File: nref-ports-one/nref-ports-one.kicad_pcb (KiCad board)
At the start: 4 copper layers, 88 x 35.5 mm, 116 parts, among them J1 CONN_HEAD, J10 CONN_SPK, J2 DM3AT-SF-PEJM5, J3 09452812561, J4 USB_C_Receptacle, J5 Conn_01x10_Pin, J6 Conn_01x14_Pin, J7 Conn_01x12_Pin, J8 PWR, J9 Conn_01x10_Pin, U1 TPS7A0533PDBZ, U12 TLV75518PDBV, U2 TLV320AIC3100, U3 TXS0108EPW, U4 SN74AVC1T45, U5 TPD4E02B04DQA, U6 TPD4E02B04DQA, U7 TPD4E02B04DQA, U8 FUSB302BMPX, U9 AP22815A

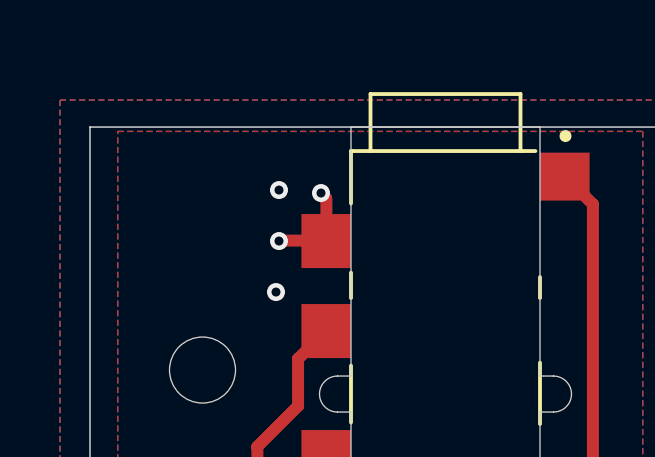
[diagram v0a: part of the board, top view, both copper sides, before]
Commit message: ports-one: schematics with new mux, local 5v, hard reset switch
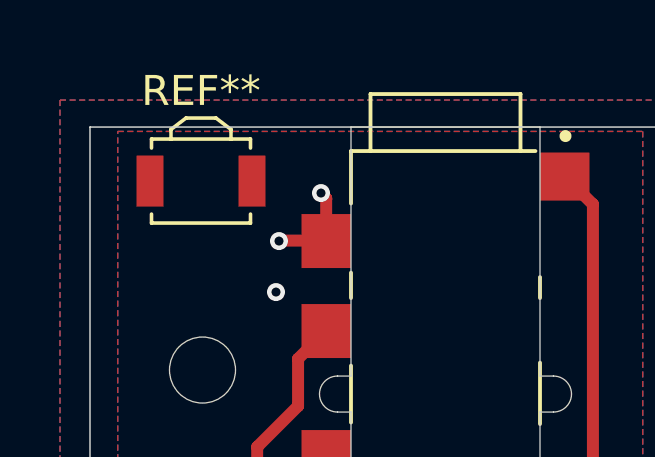
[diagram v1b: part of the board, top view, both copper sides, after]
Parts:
- added REF**: SW_SPST_B3U-3000P, Button_Switch_SMD:SW_SPST_B3U-3000P, F.Cu at (103.7, 103.7)
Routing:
- net GNDA: vias 22 -> 21

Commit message: ports-one: add redriver, routing WIP
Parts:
- removed FB10: 100@100MHz 3A, Inductor_SMD:L_0603_1608Metric
- removed REF**: SW_SPST_B3U-3000P, Button_Switch_SMD:SW_SPST_B3U-3000P
- added C45: 0.1uF, Capacitor_SMD:C_0402_1005Metric, F.Cu at (161.7, 149.2)
- added C46: 47uF, Capacitor_SMD:C_1210_3225Metric, F.Cu at (178.8, 142.3)
- added C47: 10uF, Capacitor_SMD:C_0603_1608Metric, F.Cu at (173.3, 138.6)
- added D4: LED_Blue, LED_SMD:LED_0603_1608Metric, F.Cu at (183.9, 103.7)
- added J11: POWSW, Connector_JST:JST_SH_SM02B-SRSS-TB_1x02-1MP_P1.00mm_Horizontal, F.Cu at (102.8, 131.8)
- added L4: 6.8uH, Inductor_SMD:L_Taiyo-Yuden_NR-30xx, F.Cu at (175.3, 142.2)
- added R36: 0, Resistor_SMD:R_0402_1005Metric, F.Cu at (183.8, 116.0)
- added R37: 13.7k, Resistor_SMD:R_0402_1005Metric, F.Cu at (168.7, 142.2)
- added R38: 10k, Resistor_SMD:R_0402_1005Metric, F.Cu at (166.4, 140.8)
- added R39: 0, Resistor_SMD:R_0402_1005Metric, F.Cu at (164.0, 120.5)
- added R40: 0, Resistor_SMD:R_0603_1608Metric, F.Cu at (173.1, 130.2)
- added R41: 0, Resistor_SMD:R_0402_1005Metric, F.Cu at (164.0, 121.5)
- added SW1: SW_Push, Button_Switch_SMD:SW_SPST_B3U-3000P, F.Cu at (103.8, 104.0)
- added TP1: TestPoint, TestPoint:TestPoint_Pad_D1.0mm, F.Cu at (194.4, 124.2)
- added TP2: TestPoint, TestPoint:TestPoint_Pad_D1.0mm, F.Cu at (194.4, 127.3)
- added TP3: TestPoint, TestPoint:TestPoint_Pad_D1.0mm, F.Cu at (194.4, 130.3)
- added U10: LMR51430, Package_TO_SOT_SMD:SOT-23-6, F.Cu at (171.3, 141.2)
- added U11: TPS66021YBGR, footprints:YBG0028_TEX, F.Cu at (176.9, 125.2)
- added U13: TMUXHS4212, footprints:Texas-VQFN20_2.5x4.5mm_RKS, F.Cu at (173.6, 120.5)
- added U14: EQCO5X31C0-I_6NX, footprints:QFN50P400X400X100-21N-D, F.Cu at (167.2, 131.8)
- C17, C21, C39, C40: footprint Capacitor_SMD:C_1206_3216Metric -> Capacitor_SMD:C_1210_3225Metric
- C38: value 47uF -> 0.1uF; footprint Capacitor_SMD:C_1206_3216Metric -> Capacitor_SMD:C_0402_1005Metric
- C41: value 0.1uF -> 10uF; footprint Capacitor_SMD:C_0402_1005Metric -> Capacitor_SMD:C_0603_1608Metric
- C8: value 0.1uF -> 1uF
- D1, D2: value LED_Small -> LED_Red
- D3: value SS54 -> LED_Red; footprint Diode_SMD:D_SMA -> LED_SMD:LED_0603_1608Metric
- J4: footprint footprints:MOLEX_105450-0101 -> Connector_USB:USB_C_Receptacle_Molex_105450-0101
- R23: value 200k -> 10k
- R25: value 200k -> 75k 1%
- R26: value 200k -> 0
- R27: value 200k -> 432k 1%
- R28: value 10k -> 20k 1%
- R29: value 900k -> 0
- R30: value 200k -> 2.2k
- R31: value 0 -> 2.2k
- R32, R33: value 0 -> 1k
- R34: value 10k -> 0
- R35: value 0 -> 100k
- U9: value AP22815A -> PCA9557BS; footprint Package_TO_SOT_SMD:SOT-23-5 -> Package_DFN_QFN:HVQFN-16-1EP_3x3mm_P0.5mm_EP1.5x1.5mm
- moved R34 49.0 mm to (115.2, 141.7), turned to 0 degrees
- moved C41 33.4 mm to (187.2, 144.8)
- moved R32 28.6 mm to (186.9, 104.3), turned to 90 degrees
- moved R24 28.2 mm to (184.1, 145.1), turned to 0 degrees
- moved C38 28.1 mm to (161.7, 147.2), turned to 0 degrees
- moved R21 27.9 mm to (159.1, 124.3)
- moved R29 26.4 mm to (182.1, 146.3)
- moved R33 25.0 mm to (183.7, 105.8), turned to 0 degrees
- moved R20 25.0 mm to (160.2, 124.3)
- moved D3 24.4 mm to (185.6, 103.7)
- moved R35 23.9 mm to (168.7, 140.3), turned to 90 degrees
- moved R31 21.7 mm to (156.2, 119.7), turned to -90 degrees
- moved C32 21.3 mm to (161.7, 145.2), turned to 0 degrees
- moved C40 19.4 mm to (177.8, 128.8), turned to 180 degrees
- moved R19 18.5 mm to (158.0, 124.3), turned to -90 degrees
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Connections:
- C32 pad 1: +5V -> Net-(U11-VIN)
- C37 pad 2: STANDBY_3V3 -> LDO_3V3
- C38 pad 1: MUX_5V -> Net-(U10-CB)
- C38 pad 2: GND -> Net-(U10-SW)
- C40 pad 1: USB_VBUS -> VPD
- C41 pad 1: STANDBY_3V3 -> Net-(U11-VLDO)
- C42 pad 1: MUX_3V3 -> /MUX_3V3
- C8 pad 1: +5V -> Net-(U1-VI)
- D3 pad 1: VPD -> Net-(D3-K)
- D3 pad 2: USB_VBUS -> Net-(D3-A)
- FB7 pad 1: +5V -> 5V_AUX
- R19 pad 1: Net-(U9-FLG) -> USB_SINK_EN
- R19 pad 2: +5V -> LDO_3V3
- R20 pad 1: CC2 -> ~{USB_MUX_OE}
- R21 pad 1: CC1 -> USB_MUX_DIR
- R22 pad 1: MUX_3V3 -> /MUX_3V3
- R22 pad 2: +3V3 -> STANDBY_3V3
- R23 pad 1: Net-(U10-DIR) -> GND
- R23 pad 2: MUX_3V3 -> USB_SRC_EN
- R24 pad 1: MUX_5V -> LDO_3V3
- R24 pad 2: +5V -> Net-(U11-VLDO)
- R25 pad 2: MUX_5V -> GND
- R26 pad 1: Net-(U10-~{INT_N}/OUT3) -> 5V_AUX
- R26 pad 2: MUX_5V -> Net-(U11-VIN)
- R27 pad 1: Net-(U10-VCONN_FAULT_N) -> Net-(U11-OVP)
- R27 pad 2: MUX_5V -> USB_VBUS
- R28 pad 1: MUX_5V -> Net-(U11-OVP)
- R28 pad 2: Net-(U10-CURRENT_MODE) -> GND
- R29 pad 1: USB_VBUS -> STANDBY_3V3
- R29 pad 2: Net-(U10-VBUS_DET) -> LDO_3V3
- R30 pad 1: USB_VBUS -> STANDBY_3V3
- R30 pad 2: Net-(U10-PORT) -> Net-(U9-~{RESET})
- R31 pad 1: GND -> STANDBY_3V3
- R31 pad 2: Net-(U10-~{ENN_MUX}) -> Net-(U9-A0)
- R32 pad 1: Net-(U10-SCL/OUT2) -> STANDBY_3V3
- R32 pad 2: RP_SCL0 -> Net-(D3-A)
- R33 pad 1: Net-(U10-SDA/OUT1) -> STANDBY_3V3
- R33 pad 2: RP_SDA0 -> Net-(D4-A)
- R34 pad 1: STANDBY_3V3 -> 5V_AUX
- R34 pad 2: Net-(U11-~{RESET}) -> Net-(U1-VI)
- R35 pad 1: GND -> 5V_AUX
- U1 pad 3: +5V -> Net-(U1-VI)
- U6 pad 1: USBH_2A_RXN -> /USBH_2A_AC_TXN
- U6 pad 10: USBH_2A_RXN -> /USBH_2A_AC_TXN
- U6 pad 2: USBH_2A_RXP -> /USBH_2A_AC_TXP
- U6 pad 4: /USBH_2A_AC_TXN -> USBH_2A_RXN
- U6 pad 5: /USBH_2A_AC_TXP -> USBH_2A_RXP
- U6 pad 6: /USBH_2A_AC_TXP -> USBH_2A_RXP
- U6 pad 7: /USBH_2A_AC_TXN -> USBH_2A_RXN
- U6 pad 9: USBH_2A_RXP -> /USBH_2A_AC_TXP
- U8 pad 12: unconnected-(U8-VCONN-Pad12) -> Net-(R36-Pad2)
- U8 pad 13: unconnected-(U8-VCONN-Pad13) -> Net-(R36-Pad2)
- U8 pad 3: STANDBY_3V3 -> LDO_3V3
- U8 pad 4: STANDBY_3V3 -> LDO_3V3
- U9 pad 1: USB_VBUS -> Net-(U9-A0)
- U9 pad 3: Net-(U9-FLG) -> GND
- U9 pad 5: +5V -> USB_SINK_EN
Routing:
- net +3V3: track 156.6 -> 35.1 mm, vias 6 -> 3
- net +5V: track 82.4 -> 16.4 mm, vias 3 -> 1
- net USB1_TXN: track 0.00 -> 55.4 mm
- net USB1_TXP: track 0.00 -> 54.3 mm
- net USB1_RXN: track 0.00 -> 51.4 mm, vias 1 -> 0
- net USB1_RXP: track 0.00 -> 50.8 mm
- net +1V8: track 49.9 -> 8.60 mm
- net GND: track 89.8 -> 51.1 mm, vias 66 -> 39
- net ETH0_LED_LINK1: track 32.9 -> 0.00 mm
- net DAC_SDA: track 34.9 -> 3.16 mm
- net DAC_SCL: track 35.1 -> 3.67 mm
- net ETH0_LED_RX: track 30.4 -> 0.00 mm
- net USB_VBUS: track 38.0 -> 12.4 mm, vias 7 -> 3
- net Net-(U13-SEL): track 23.4 -> 0.00 mm, vias 1 -> 0
- net Net-(U2-DIN): track 26.0 -> 2.70 mm
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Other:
- board text added: "TODO: caps might be too high"

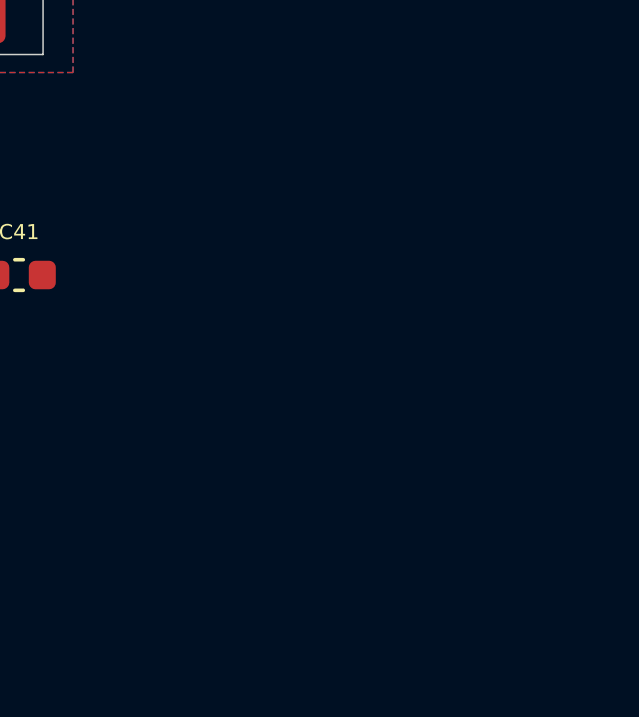
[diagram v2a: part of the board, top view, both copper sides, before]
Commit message: ports-one: add redriver circuit
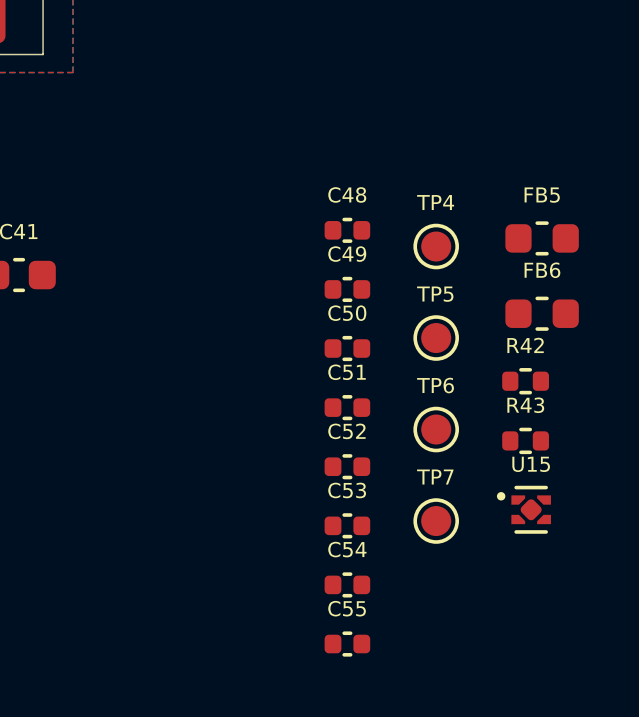
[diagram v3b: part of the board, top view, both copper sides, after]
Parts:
- added C48: 1uF, Capacitor_SMD:C_0402_1005Metric, F.Cu at (198.1, 143.3)
- added C49: 1uF, Capacitor_SMD:C_0402_1005Metric, F.Cu at (198.1, 145.2)
- added C50: 4.7uF, Capacitor_SMD:C_0402_1005Metric, F.Cu at (198.1, 147.2)
- added C51: 4.7uF, Capacitor_SMD:C_0402_1005Metric, F.Cu at (198.1, 149.2)
- added C52: 0.1uF, Capacitor_SMD:C_0402_1005Metric, F.Cu at (198.1, 151.1)
- added C53: 1uF, Capacitor_SMD:C_0402_1005Metric, F.Cu at (198.1, 153.1)
- added C54: 1uF, Capacitor_SMD:C_0402_1005Metric, F.Cu at (198.1, 155.1)
- added C55: 0.1uF, Capacitor_SMD:C_0402_1005Metric, F.Cu at (198.1, 157.1)
- added FB5: 100@100MHz 3A, Inductor_SMD:L_0603_1608Metric, F.Cu at (204.6, 143.5)
- added FB6: 100@100MHz 3A, Inductor_SMD:L_0603_1608Metric, F.Cu at (204.6, 146.0)
- added R42: 0, Resistor_SMD:R_0402_1005Metric, F.Cu at (204.1, 148.3)
- added R43: 0, Resistor_SMD:R_0402_1005Metric, F.Cu at (204.1, 150.3)
- added TP4: TestPoint, TestPoint:TestPoint_Pad_D1.0mm, F.Cu at (201.1, 143.8)
- added TP5: TestPoint, TestPoint:TestPoint_Pad_D1.0mm, F.Cu at (201.1, 146.8)
- added TP6: TestPoint, TestPoint:TestPoint_Pad_D1.0mm, F.Cu at (201.1, 149.9)
- added TP7: TestPoint, TestPoint:TestPoint_Pad_D1.0mm, F.Cu at (201.1, 152.9)
- added U15: LP5907MFX-1.2, Package_SON:Texas_X2SON-4_1x1mm_P0.65mm, F.Cu at (204.3, 152.6)
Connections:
- U14 pad 10: unconnected-(U14-TSI-Pad10) -> Net-(U14-TSI)
- U14 pad 11: unconnected-(U14-LOM-Pad11) -> Net-(U14-LOM)
- U14 pad 14: unconnected-(U14-VCCB-Pad14) -> +1V2
- U14 pad 15: unconnected-(U14-PLLB1-Pad15) -> Net-(U14-PLLB1)
- U14 pad 16: unconnected-(U14-PLLB2-Pad16) -> Net-(U14-PLLB2)
- U14 pad 20: unconnected-(U14-TEST0-Pad20) -> Net-(U14-TEST0)
- U14 pad 4: unconnected-(U14-VCCA-Pad4) -> +1V2
- U14 pad 5: unconnected-(U14-PLLA1-Pad5) -> Net-(U14-PLLA1)
- U14 pad 6: unconnected-(U14-PLLA2-Pad6) -> Net-(U14-PLLA2)
- U14 pad 7: unconnected-(U14-TSC-Pad7) -> Net-(U14-TSC)

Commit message: ports-one: routing snapshot
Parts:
- removed R24: 0, Resistor_SMD:R_0402_1005Metric
- removed TP7: TestPoint, TestPoint:TestPoint_Pad_D1.0mm
- FB1, FB2, FB3, FB4, FB5, FB6, FB7, FB8, FB9: footprint Inductor_SMD:L_0603_1608Metric -> Inductor_SMD:L_0402_1005Metric
- moved FB5 43.8 mm to (163.5, 128.3), turned to 90 degrees
- moved TP1 42.4 mm to (152.3, 119.5)
- moved TP2 41.6 mm to (153.2, 121.0)
- moved TP6 41.5 mm to (167.8, 125.2)
- moved C53 41.1 mm to (165.4, 128.3), turned to 90 degrees
- moved TP4 40.8 mm to (162.4, 130.7)
- moved TP5 40.7 mm to (166.2, 125.9)
- moved C52 40.7 mm to (164.4, 128.3), turned to 90 degrees
- moved R43 40.3 mm to (169.2, 130.1), turned to 90 degrees
- moved C50 40.2 mm to (162.5, 128.7), turned to -90 degrees
- moved U15 37.5 mm to (171.5, 134.2), turned to 180 degrees
- moved FB6 37.4 mm to (168.7, 135.6), turned to 90 degrees
- moved C55 37.2 mm to (167.8, 135.6), turned to -90 degrees
- moved C54 36.9 mm to (166.8, 135.6), turned to -90 degrees
- moved R42 36.0 mm to (171.6, 132.9)
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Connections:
- net USBH_2B_TXN renamed USB_A_TXN
- net USBH_2B_TXP renamed USB_A_TXP
- C33 pad 1: /USBH_2A_AC_TXN -> /USB_B_AC_TXN
- C33 pad 2: USBH_2A_TXN -> USB_B_TXN
- C34 pad 1: /USBH_2B_AC_TXN -> /USB_A_AC_TXN
- C35 pad 1: /USBH_2A_AC_TXP -> /USB_B_AC_TXP
- C35 pad 2: USBH_2A_TXP -> USB_B_TXP
- C36 pad 1: /USBH_2B_AC_TXP -> /USB_A_AC_TXP
- C41 pad 1: Net-(U11-VLDO) -> LDO_3V3
- J4 pad A10: USBH_2B_RXN -> USB_A_RXN
- J4 pad A11: USBH_2B_RXP -> USB_A_RXP
- J4 pad A2: /USBH_2A_AC_TXP -> /USB_B_AC_TXP
- J4 pad A3: /USBH_2A_AC_TXN -> /USB_B_AC_TXN
- J4 pad B10: USBH_2A_RXN -> USB_B_RXN
- J4 pad B11: USBH_2A_RXP -> USB_B_RXP
- J4 pad B2: /USBH_2B_AC_TXP -> /USB_A_AC_TXP
- J4 pad B3: /USBH_2B_AC_TXN -> /USB_A_AC_TXN
- U11 pad G3: Net-(U11-VLDO) -> LDO_3V3
- U13 pad 12: USBH_2A_TXN -> USB_B_TXP
- U13 pad 13: USBH_2A_TXP -> USB_B_TXN
- U13 pad 14: USBH_2B_RXN -> USB_B_RXP
- U13 pad 15: USBH_2B_RXP -> USB_B_RXN
- U13 pad 18: USBH_2A_RXN -> USB_A_RXN
- U13 pad 19: USBH_2A_RXP -> USB_A_RXP
- U6 pad 1: /USBH_2A_AC_TXN -> USB_B_RXN
- U6 pad 10: /USBH_2A_AC_TXN -> USB_B_RXN
- U6 pad 2: /USBH_2A_AC_TXP -> USB_B_RXP
- U6 pad 4: USBH_2A_RXN -> /USB_B_AC_TXN
- U6 pad 5: USBH_2A_RXP -> /USB_B_AC_TXP
- U6 pad 6: USBH_2A_RXP -> /USB_B_AC_TXP
- U6 pad 7: USBH_2A_RXN -> /USB_B_AC_TXN
- U6 pad 9: /USBH_2A_AC_TXP -> USB_B_RXP
- U7 pad 1: USBH_2B_RXN -> /USB_A_AC_TXN
- U7 pad 10: USBH_2B_RXN -> /USB_A_AC_TXN
- U7 pad 2: USBH_2B_RXP -> /USB_A_AC_TXP
- U7 pad 4: /USBH_2B_AC_TXN -> USB_A_RXN
- U7 pad 5: /USBH_2B_AC_TXP -> USB_A_RXP
- U7 pad 6: /USBH_2B_AC_TXP -> USB_A_RXP
- U7 pad 7: /USBH_2B_AC_TXN -> USB_A_RXN
- U7 pad 9: USBH_2B_RXP -> /USB_A_AC_TXP
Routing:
- net USB1_DN: track 1.61 -> 95.2 mm, vias 0 -> 2
- net USB1_DP: track 1.63 -> 95.2 mm, vias 2 -> 4
- net Net-(J10-Pin_2): track 0.95 -> 71.3 mm
- net Net-(J10-Pin_1): track 0.95 -> 60.3 mm, vias 1 -> 2
- net ETH0_LED_RX: track 0.00 -> 37.0 mm, vias 0 -> 4
- net ETH0_LED_LINK1: track 0.00 -> 36.8 mm, vias 0 -> 4
- net Net-(D3-K): track 0.00 -> 35.6 mm, vias 0 -> 2
- net Net-(D4-K): track 0.00 -> 33.7 mm, vias 0 -> 2
- net DAC_SDA: track 3.16 -> 27.8 mm
- net DAC_SCL: track 3.67 -> 27.0 mm
- net Net-(U2-DOUT): track 2.19 -> 25.3 mm
- net VCC: track 0.00 -> 22.6 mm, vias 0 -> 6
- net Net-(U2-DIN): track 2.70 -> 25.2 mm
- net Net-(U13-SEL): track 0.00 -> 22.0 mm, vias 0 -> 2
- net GND: track 51.1 -> 71.3 mm, vias 39 -> 83
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- added copper zone on F.Cu, net USB_VBUS
- added copper zone on B.Cu, net VPD
- added copper zone on F.Cu, net VPD

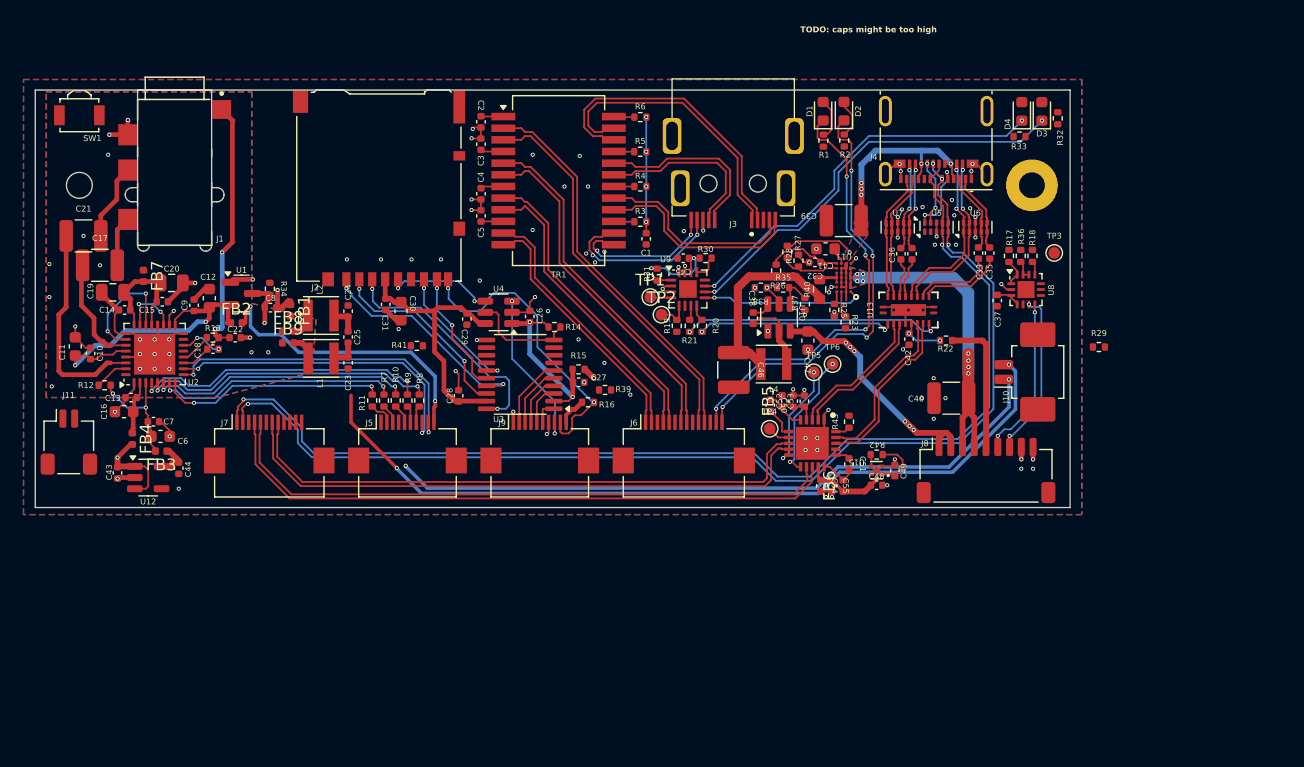
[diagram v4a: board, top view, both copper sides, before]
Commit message: WIP nref-ports-one: routing done, 3d checks to do
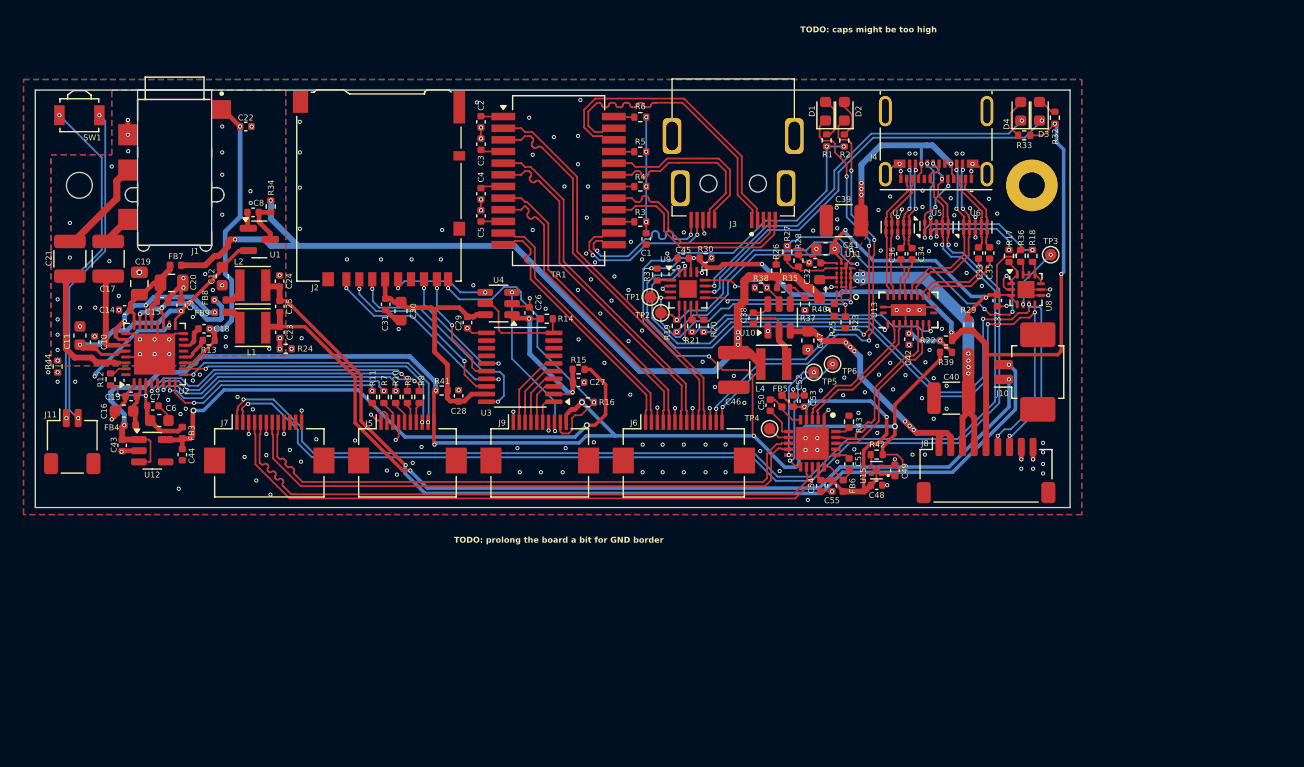
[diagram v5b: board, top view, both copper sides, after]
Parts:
- removed FB1: 100@100MHz 3A, Inductor_SMD:L_0402_1005Metric
- removed FB2: DNP, Inductor_SMD:L_0402_1005Metric
- added R24: 0, Resistor_SMD:R_0402_1005Metric, F.Cu at (121.3, 123.9)
- added R44: 0, Resistor_SMD:R_0402_1005Metric, F.Cu at (101.9, 125.4)
- moved R39 29.2 mm to (177.4, 124.2)
- moved C22 18.0 mm to (117.9, 105.0)
- moved R29 11.3 mm to (179.3, 121.9), turned to 90 degrees
- moved C8 8.23 mm to (118.5, 112.3), turned to 180 degrees
- moved R34 7.00 mm to (120.0, 111.8)
- moved L1 6.36 mm to (118.5, 122.1)
- moved C24 6.36 mm to (120.8, 118.2)
- moved C25 6.36 mm to (120.8, 120.3)
- moved C23 6.36 mm to (120.8, 122.5)
- moved FB8 6.35 mm to (115.7, 119.8)
- moved L2 6.34 mm to (118.5, 118.5)
- moved FB9 6.31 mm to (115.8, 120.8)
- moved U1 4.84 mm to (119.0, 114.6)
- moved R41 4.35 mm to (134.6, 127.5), turned to 180 degrees
- moved FB7 2.89 mm to (112.0, 116.8), turned to 180 degrees
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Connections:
- C8 pad 2: GND -> GNDA
- U1 pad 1: GND -> GNDA
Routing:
- net +3V3: track 39.8 -> 155.2 mm, vias 3 -> 9
- net 5V_AUX: track 16.7 -> 77.7 mm, vias 0 -> 5
- net STANDBY_3V3: track 19.3 -> 73.4 mm, vias 2 -> 6
- net RP_SDA0: track 14.2 -> 63.3 mm, vias 3 -> 4
- net RP_SCL0: track 14.7 -> 63.6 mm, vias 3 -> 4
- net +1V8: track 4.22 -> 48.7 mm, vias 1 -> 2
- net LDO_3V3: track 3.67 -> 45.8 mm, vias 0 -> 4
- net Net-(J11-Pin_1): track 0.00 -> 28.6 mm, vias 0 -> 2
- net Net-(J11-Pin_2): track 0.00 -> 27.6 mm, vias 0 -> 2
- net USB_VBUS: track 30.7 -> 51.5 mm, vias 7 -> 10
- net USB_SINK_EN: track 3.39 -> 23.3 mm, vias 1 -> 2
- net USB_SRC_EN: track 4.02 -> 23.5 mm, vias 0 -> 2
- net Net-(J10-Pin_1): track 60.3 -> 78.1 mm
- net +1V2: track 11.1 -> 26.3 mm, vias 0 -> 2
- net Net-(FB8-Pad1): track 23.1 -> 12.2 mm
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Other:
- board text added: "TODO: prolong the board a bit for GND border"
